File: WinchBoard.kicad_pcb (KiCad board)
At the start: 2 copper layers, 0 parts

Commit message: Checkpoint
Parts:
- added FID1: Fiducial_Top, _Connector:Fiducial_0.040_Top, F.Cu at (102.8, 74.2)
- added FID2: Fiducial_Top, _Connector:Fiducial_0.040_Top, F.Cu at (146.2, 81.3)
- added FID3: Fiducial_Top, _Connector:Fiducial_0.040_Top, F.Cu at (125.8, 106.4)
- added H1: HOLE_GNDD, _Connector:MountingHole_3.2mm_M3, F.Cu at (105.4, 69.8)
- added H2: HOLE_GNDD, _Connector:MountingHole_3.2mm_M3, F.Cu at (105.4, 97.8)
- added H3: HOLE_GNDD, _Connector:MountingHole_3.2mm_M3, F.Cu at (144.4, 69.3)
- added H4: HOLE_GNDD, _Connector:MountingHole_3.2mm_M3, F.Cu at (134.2, 106.2)
- added J1: HDMI_A, _Connector:FCI_10029449-11[13]RLF, F.Cu at (110.0, 83.8)
- added P1: CONN_01X04, _Connector:Molex_KK-6410-04_04x2.54mm_Straight, F.Cu at (128.0, 83.5)
- added P2: CONN_01X04, _Connector:Molex_KK-6410-04_04x2.54mm_Straight, F.Cu at (128.0, 90.6)
- added P3: CONN_01X04, _Connector:Molex_KK-6410-04_04x2.54mm_Straight, F.Cu at (128.0, 97.8)
- added P4: CONN_01X02, _Connector:Molex_KK-6410-02_02x2.54mm_Straight, F.Cu at (125.6, 76.3)
- added P5: CONN_01X02, _Connector:Molex_KK-6410-02_02x2.54mm_Straight, F.Cu at (132.1, 76.3)
- added P6: CONN_01X02, _Connector:0.100_1x2_small, F.Cu at (125.9, 69.3)
- added P7: CONN_01X03, _Connector:0.100_1x3_small, F.Cu at (117.2, 99.5)
- added TT1: SCL1, _Connector:Test_Point_SMD_0.040_Top, F.Cu at (140.0, 88.2)
- added TT10: Aout, _Connector:Test_Point_SMD_0.040_Top, F.Cu at (111.2, 99.5)
- added TT11: +Vanalog, _Connector:Test_Point_SMD_0.040_Top, F.Cu at (111.3, 96.2)
- added TT2: SDA1, _Connector:Test_Point_SMD_0.040_Top, F.Cu at (119.6, 65.0)
- added TT3: SCL2, _Connector:Test_Point_SMD_0.040_Top, F.Cu at (122.7, 64.9)
- added TT4: SDA2, _Connector:Test_Point_SMD_0.040_Top, F.Cu at (126.2, 65.0)
- added TT5: SCL3, _Connector:Test_Point_SMD_0.040_Top, F.Cu at (130.7, 65.0)
- added TT6: SDA3, _Connector:Test_Point_SMD_0.040_Top, F.Cu at (134.4, 64.2)
- added TT7: DI1, _Connector:Test_Point_SMD_0.040_Top, F.Cu at (124.3, 60.9)
- added TT8: DI2, _Connector:Test_Point_SMD_0.040_Top, F.Cu at (129.3, 61.1)
- added TT9: +3.3v, _Connector:Test_Point_SMD_0.040_Top, F.Cu at (138.8, 60.9)

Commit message: Checkpoint - component placement
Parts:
- added TT10: GND, _Connector:Test_Point_SMD_0.040_Top, F.Cu at (137.2, 90.8)
- added TT12: GND, _Connector:Test_Point_SMD_0.040_Top, F.Cu at (137.2, 80.0)
- added TT13: GNDA, _Connector:Test_Point_SMD_0.040_Top, F.Cu at (111.1, 96.5)
- moved FID3 39.3 mm to (134.0, 67.9)
- moved TT6 30.4 mm to (135.3, 94.6)
- moved TT5 28.1 mm to (135.3, 92.7)
- moved TT4 25.6 mm to (135.3, 88.9)
- moved TT3 25.4 mm to (135.3, 87.0)
- moved TT9 24.9 mm to (137.2, 85.7)
- moved TT2 24.5 mm to (135.3, 83.8)
- moved TT7 18.6 mm to (136.5, 74.9)
- moved TT8 17.9 mm to (136.5, 77.5)
- moved FID2 13.7 mm to (141.0, 94.0)
- moved H4 9.45 mm to (138.4, 97.8)
- moved TT1 7.85 mm to (135.3, 81.9)
- moved H3 6.02 mm to (138.4, 69.8)
- moved TT14 2.19 mm to (111.1, 94.0)
- moved P6 0.79 mm to (125.7, 68.6)
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- renumbered TT10 to TT11, TT11 to TT14
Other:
- board outline added: 40.6 x 35.6 mm

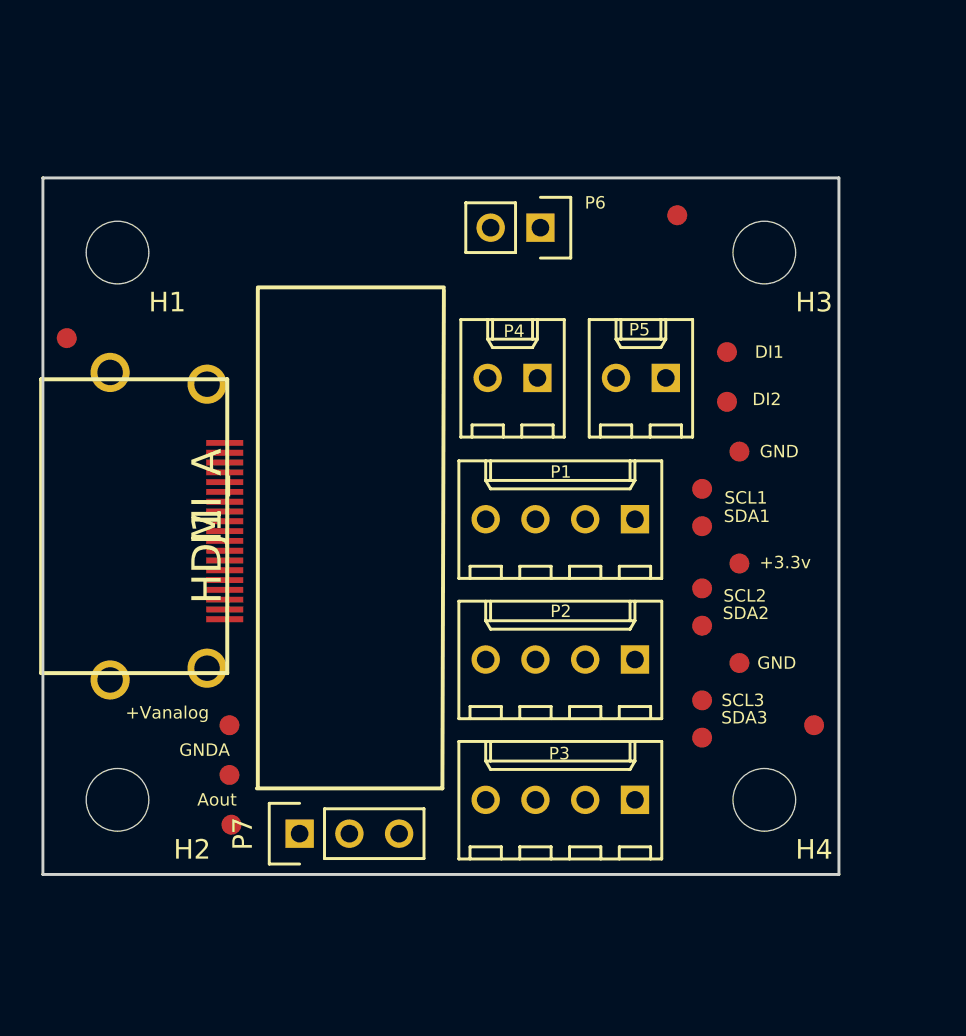
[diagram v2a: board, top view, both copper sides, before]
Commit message: Version 001 - 1.4” x 1/6” locking connectors
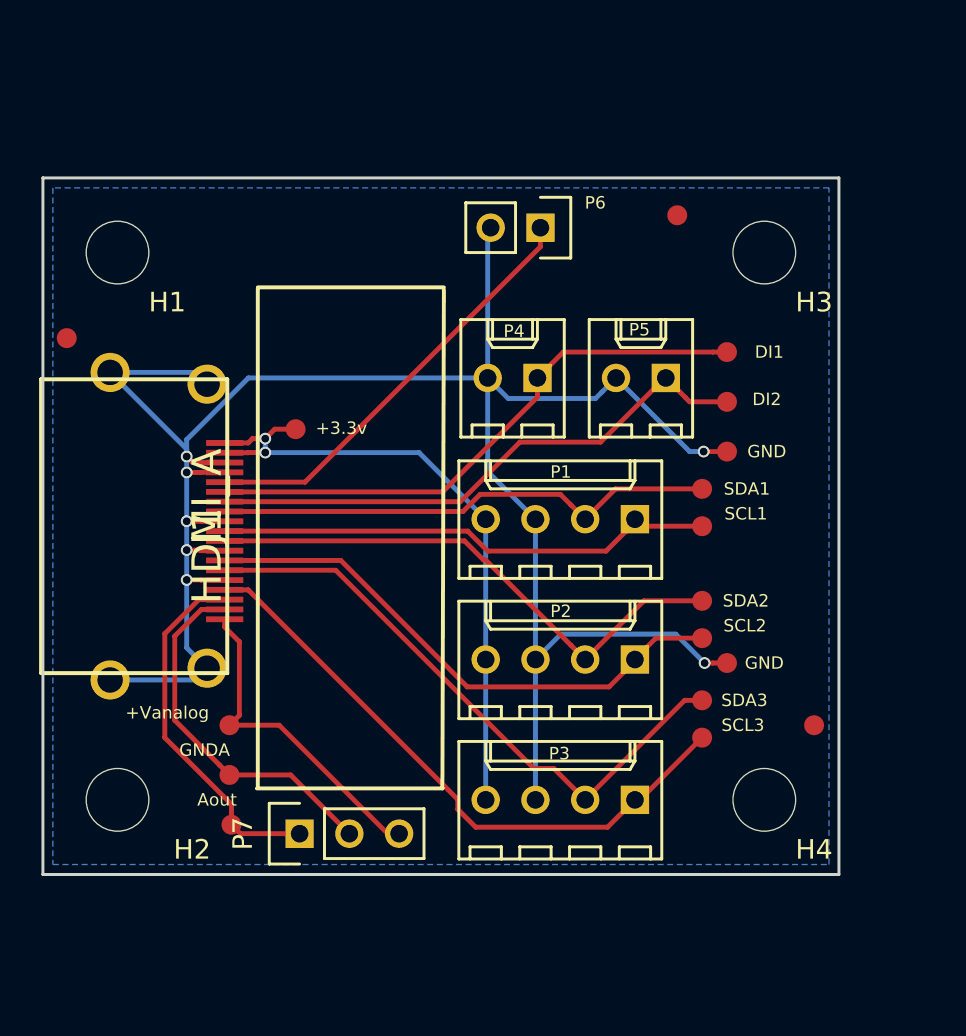
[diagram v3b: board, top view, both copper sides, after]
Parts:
- moved TT9 23.7 mm to (114.5, 78.9)
- moved TT3 2.54 mm to (135.3, 89.5)
- moved TT5 1.91 mm to (135.3, 94.6)
- moved TT6 1.91 mm to (135.3, 92.7)
- moved TT1 1.90 mm to (135.3, 83.8)
- moved TT2 1.90 mm to (135.3, 81.9)
- moved TT4 1.27 mm to (135.3, 87.6)
- moved TT10 0.63 mm to (136.5, 90.8)
- moved TT12 0.63 mm to (136.5, 80.0)
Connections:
- J1 pad 13: /Main/DO -> /Main/DI2
- J1 pad 15: /Main/DI2 -> /Main/DO
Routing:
- net GNDD: track 0.00 -> 110.8 mm, vias 0 -> 7
- net +3V3: track 0.00 -> 33.7 mm, vias 0 -> 2
- net /Main/SCL3: track 0.00 -> 31.6 mm
- net /Main/SDA3: track 0.00 -> 31.3 mm
- net /Main/DI1: track 0.00 -> 29.2 mm
- net /Main/DI2: track 0.00 -> 28.8 mm
- net /Main/SCL2: track 0.00 -> 28.1 mm
- net /Main/SDA2: track 0.00 -> 28.1 mm
- net /Main/SDA1: track 0.00 -> 25.9 mm
- net /Main/SCL1: track 0.00 -> 25.7 mm
- net /Main/DO: track 0.00 -> 22.1 mm
- net GNDA: track 0.00 -> 18.7 mm
- net /Main/Aout: track 0.00 -> 18.6 mm
- net +Vanalog: track 0.00 -> 16.9 mm
- added copper zone on B.Cu, net GNDD

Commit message: Double sided done for now.
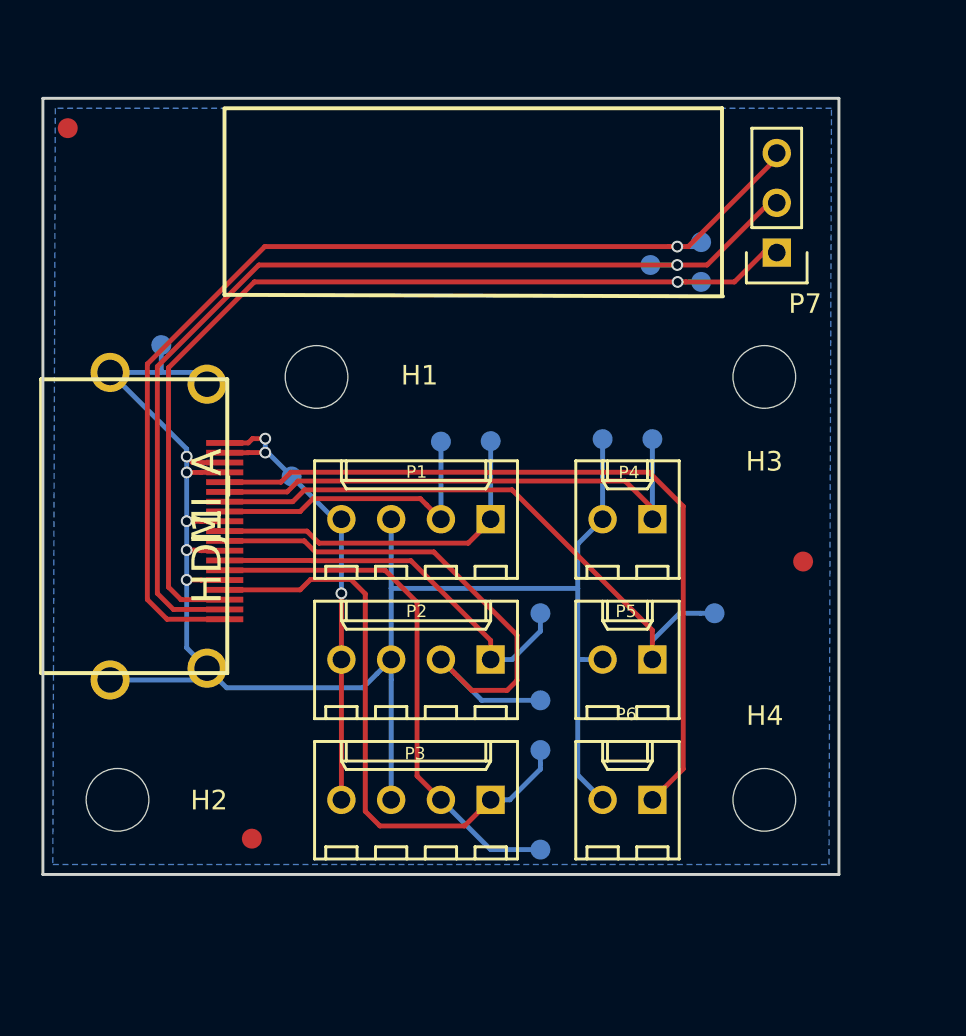
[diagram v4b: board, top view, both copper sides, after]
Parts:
- P6: footprint _Connector:0.100_1x2_small -> _Connector:Molex_KK-6410-02_02x2.54mm_Straight
- TT1, TT10, TT11, TT12, TT13, TT14, TT2, TT3, TT4, TT5, TT6, TT7, TT8, TT9: footprint _Connector:Test_Point_SMD_0.040_Top -> _Connector:Test_Point_SMD_0.040_Bottom
- moved P7 38.9 mm to (139.1, 67.3), turned to 180 degrees
- moved TT11 36.6 mm to (135.2, 71.3)
- moved TT14 34.5 mm to (135.2, 69.3)
- moved TT13 33.8 mm to (132.6, 70.5)
- moved FID3 31.4 mm to (102.9, 63.5)
- moved P6 29.8 mm to (131.4, 97.8), turned to 180 degrees
- moved TT12 29.4 mm to (107.6, 74.6)
- moved FID1 27.2 mm to (112.3, 99.8)
- moved P5 14.4 mm to (131.4, 90.6)
- moved TT2 13.6 mm to (121.9, 79.5)
- moved TT10 13.1 mm to (130.2, 79.4)
- moved H1 12.0 mm to (115.6, 76.2)
- moved TT1 11.6 mm to (124.5, 79.5)
- moved TT6 11.2 mm to (127.0, 100.3)
- moved TT8 10.8 mm to (135.9, 88.3)
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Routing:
- net +Vanalog: track 16.9 -> 54.4 mm, vias 0 -> 1
- net GNDA: track 18.7 -> 51.8 mm, vias 0 -> 1
- net /Main/Aout: track 18.6 -> 49.0 mm, vias 0 -> 1
- net /Main/DO: track 22.1 -> 40.0 mm
- net GNDD: track 110.8 -> 93.8 mm, vias 7 -> 5
- net /Main/SDA1: track 25.9 -> 15.7 mm
- net +3V3: track 33.7 -> 24.6 mm, vias 2 -> 3
- net /Main/SCL2: track 28.1 -> 20.3 mm
- net /Main/SCL1: track 25.7 -> 18.4 mm
- net /Main/SDA3: track 31.3 -> 27.2 mm
- net /Main/DI2: track 28.8 -> 31.3 mm
- net /Main/DI1: track 29.2 -> 27.3 mm
- net /Main/SDA2: track 28.1 -> 29.9 mm
- net /Main/SCL3: track 31.6 -> 30.2 mm
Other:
- board size 40.6 x 35.6 mm -> 40.6 x 39.6 mm
- board text added: "1"
- board text added: "2"
- board text added: "3"
- board text added: "HDMI Cable"
- board text added: "I2C Ports"
- board text added: "IN #1"
- board text added: "IN #2"
- board text added: "IO Ports"
- board text added: "Load Cell"
- board text added: "OUT"

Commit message: Semi-final commit before fab
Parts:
- moved TT2 8.33 mm to (127.3, 85.9)
- moved TT7 5.07 mm to (135.6, 83.6)
- moved TT1 5.04 mm to (127.3, 83.6)
- moved TT5 2.69 mm to (127.3, 97.9)
- moved TT8 2.48 mm to (135.7, 90.7)
- moved TT3 2.43 mm to (127.3, 90.7)
- moved TT4 0.50 mm to (127.3, 93.1)
- moved TT6 0.34 mm to (127.3, 100.2)
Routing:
- net /Main/SDA1: track 15.7 -> 18.1 mm
- net /Main/DI2: track 31.3 -> 29.6 mm
- net /Main/SCL3: track 30.2 -> 29.0 mm
- net /Main/DI1: track 27.3 -> 26.1 mm
- net /Main/SCL2: track 20.3 -> 19.1 mm
- net /Main/SCL1: track 18.4 -> 17.3 mm
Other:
- board text added: "Winch Signal Breakout revA"

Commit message: Submitted for fab
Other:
- rule pad_to_mask_clearance: 0.2 -> 0.0762
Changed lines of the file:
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@@
     (pad_size 1.524 1.524)
     (pad_drill 0.762)
-    (pad_to_mask_clearance 0.2)
+    (pad_to_mask_clearance 0.0762)
+    (solder_mask_min_width 0.0254)
+    (pad_to_paste_clearance -0.0254)
     (aux_axis_origin 0 0)
     (visible_elements FFFFFF7F)
     (pcbplotparams
-      (layerselection 0x00030_80000001)
+      (layerselection 0x010fc_80000001)
       (usegerberextensions false)
       (excludeedgelayer true)
@@
       (psnegative false)
       (psa4output false)
-      (plotreference true)
+      (plotreference false)
       (plotvalue true)
       (plotinvisibletext false)
@@
       (outputformat 1)
       (mirror false)
-      (drillshape 1)
+      (drillshape 0)
       (scaleselection 1)
-      (outputdirectory ""))
+      (outputdirectory ProjectOutputs/))
   )
   (net 0 "")
